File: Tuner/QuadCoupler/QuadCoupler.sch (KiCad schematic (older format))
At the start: 109 parts, among them J1 Conn_01x01, J10 Conn_01x02, J11 Conn_01x01, J12 Conn_01x01, J13 Conn_01x01, J14 Conn_01x01, J15 Conn_01x01, J16 Conn_01x01, J17 Conn_01x01, J19 Conn_01x02, J2 Conn_Coaxial, J21 Conn_01x01, J22 Conn_01x01, J23 Conn_01x01, J24 Conn_01x01, J3 Conn_Coaxial, J4 Conn_Coaxial, J5 Conn_Coaxial, J6 Conn_Coaxial, J7 Conn_01x01, J8 Conn_01x01, J9 Conn_01x01

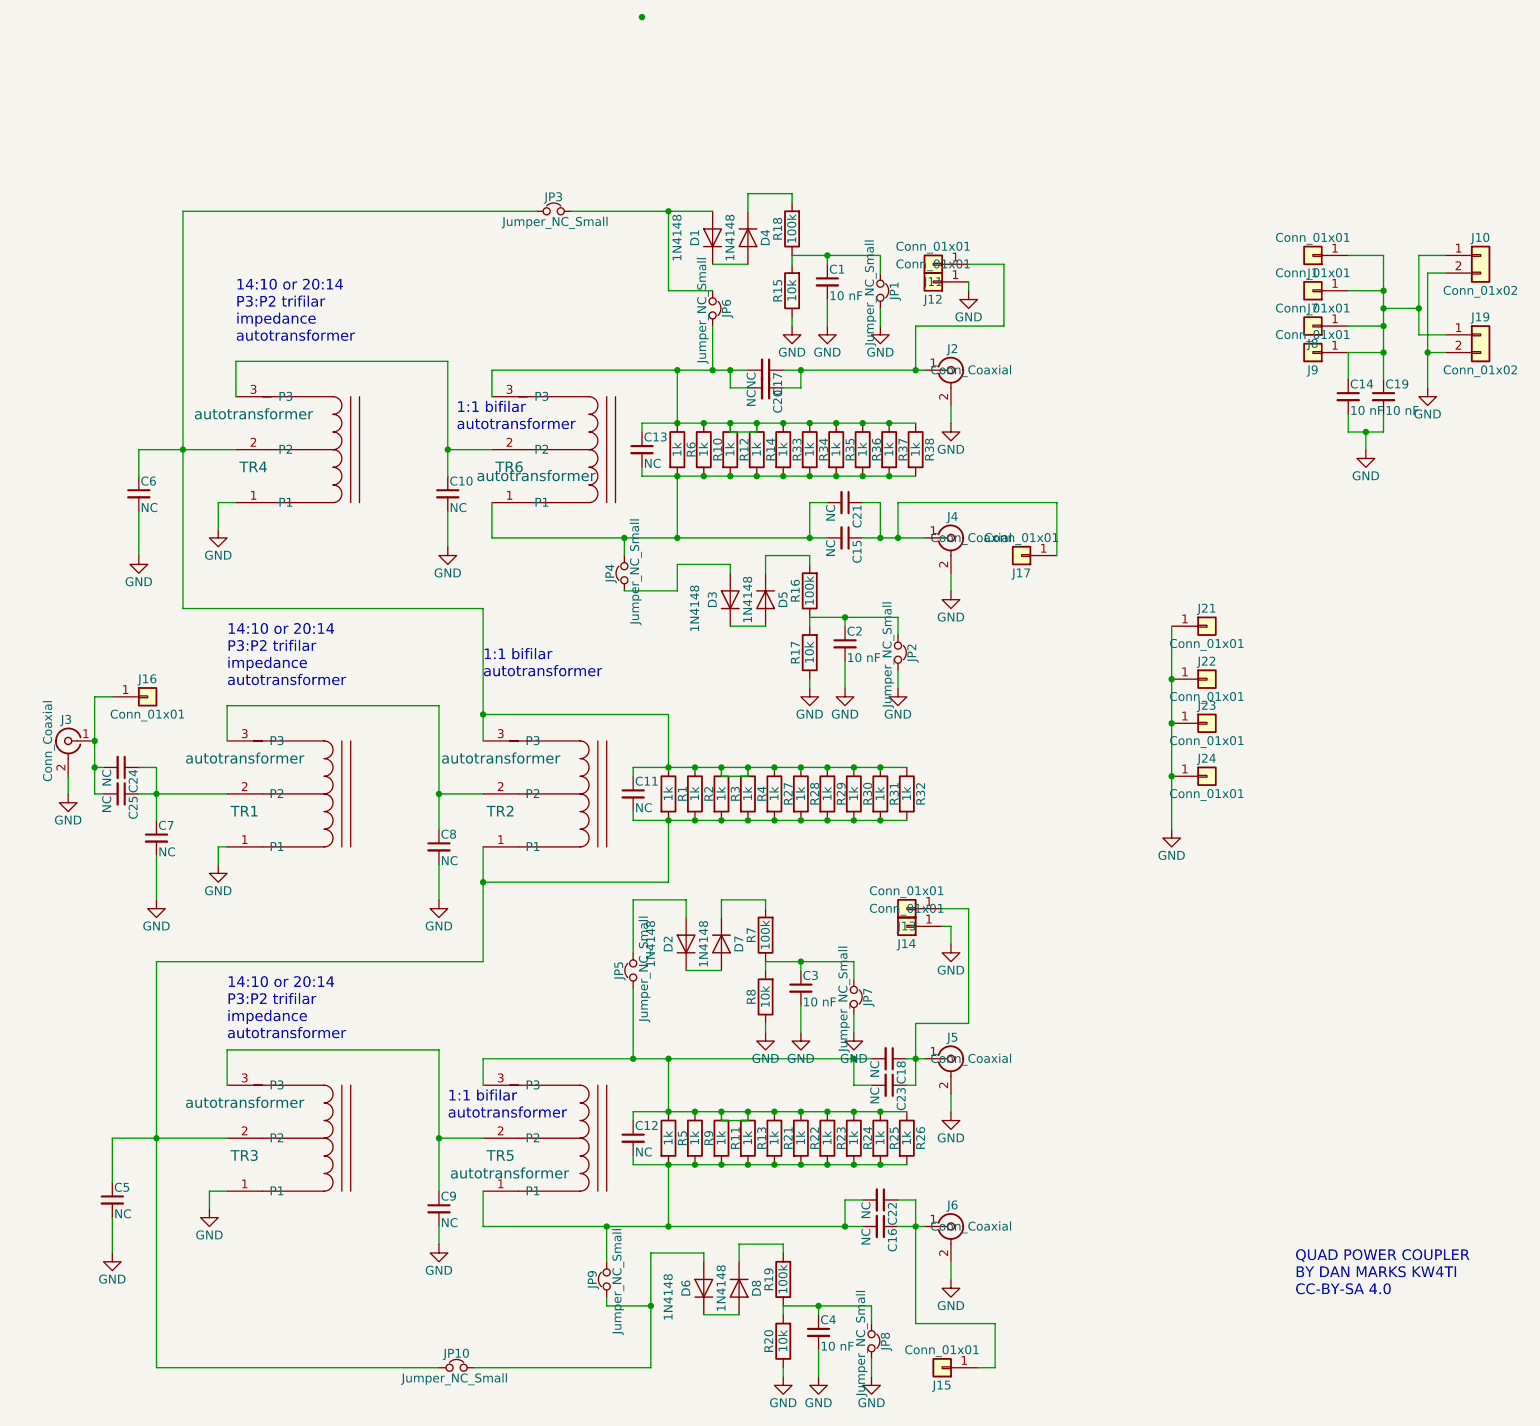
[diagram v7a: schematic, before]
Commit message: Change named to DirectionalCoupler, fixed order of two pins in QuadCoupler
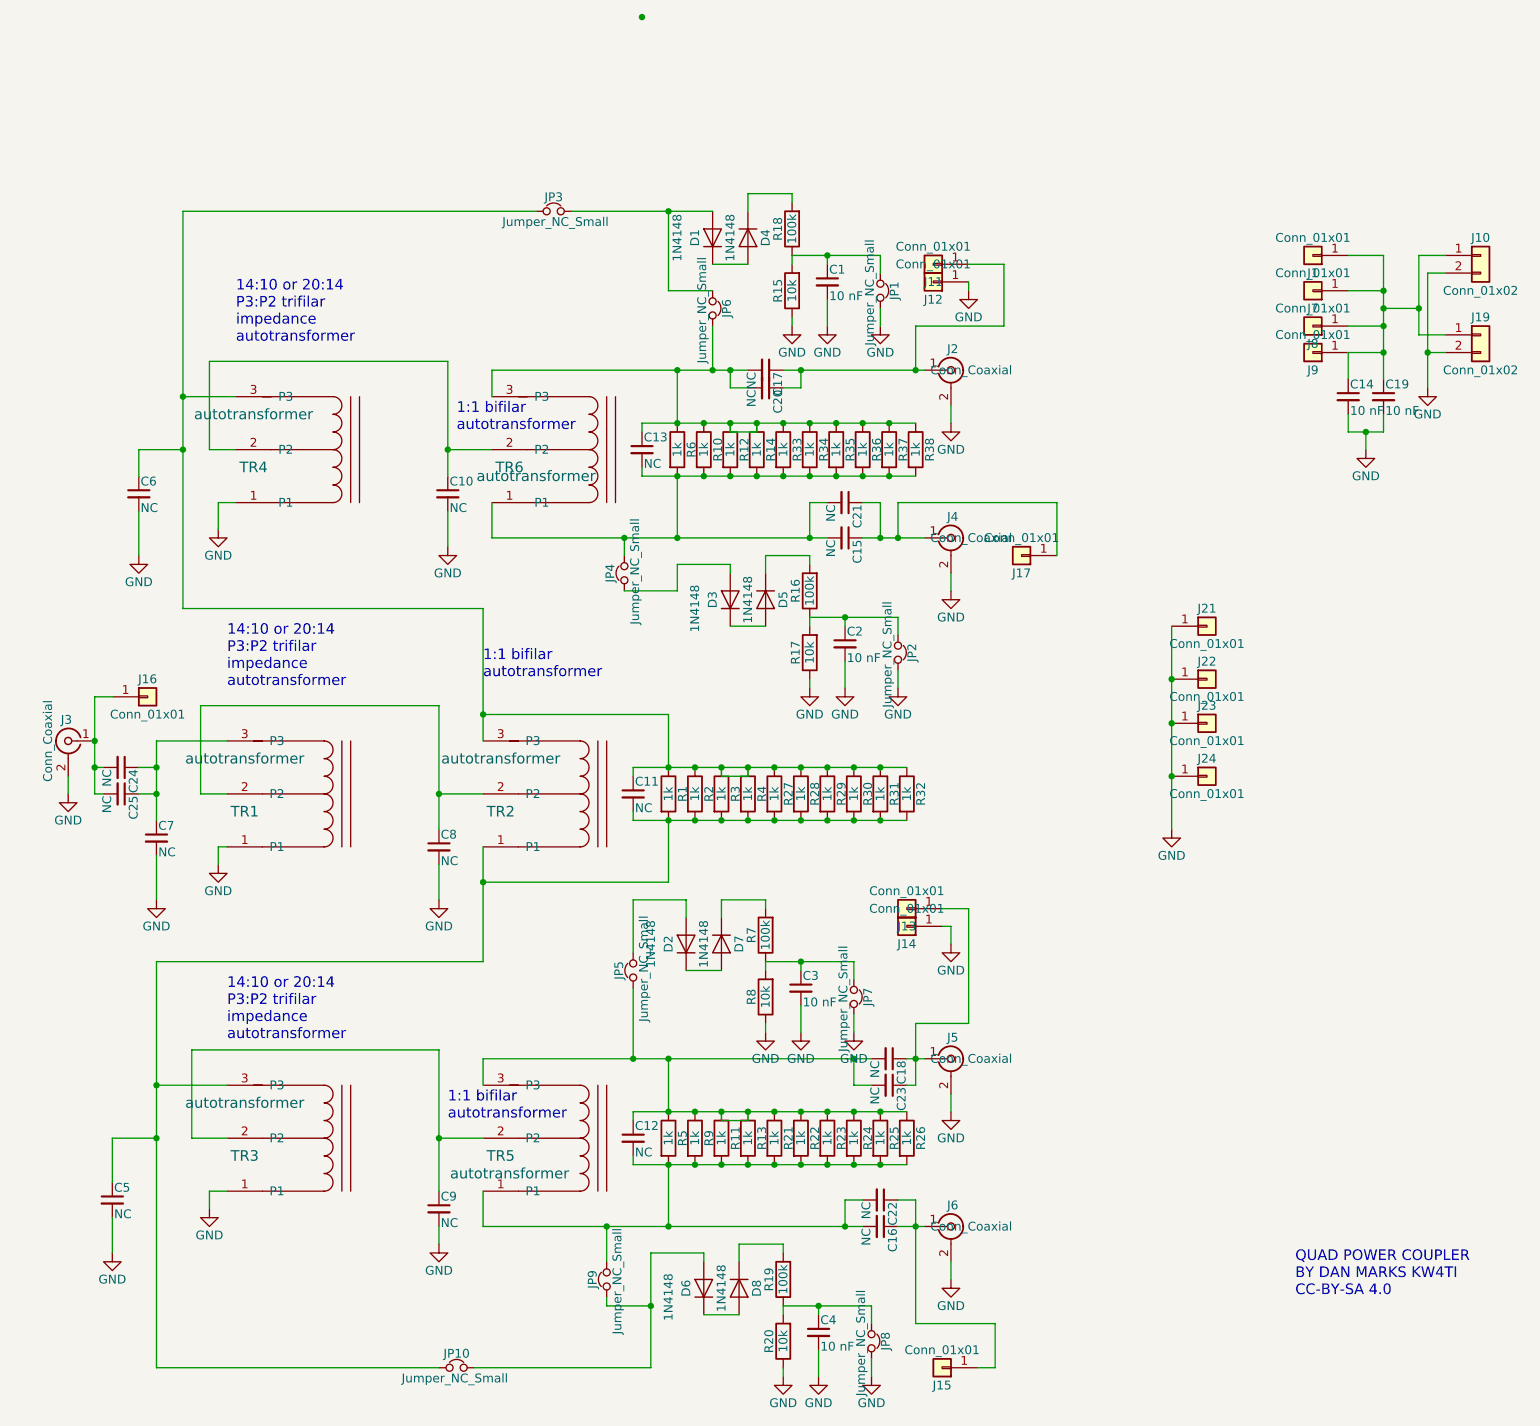
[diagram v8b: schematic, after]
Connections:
- net at C24.1, C25.1, C7.1: now also TR1.3 (P3); no longer TR1.2 (P2)
- net at C8.1, TR2.2 (P2): now also TR1.2 (P2); no longer TR1.3 (P3)
- net at C11.2, C5.1, JP10.2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: now also TR3.3 (P3); no longer TR3.2 (P2)
- net at C11.1, C6.1, JP3.1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: now also TR4.3 (P3); no longer TR4.2 (P2)
- net at C10.1, TR6.2 (P2): now also TR4.2 (P2); no longer TR4.3 (P3)
- net at C9.1, TR5.2 (P2): now also TR3.2 (P2); no longer TR3.3 (P3)
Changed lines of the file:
@@
 $EndComp
 $Comp
-L GND #PWR29
+L GND #PWR01
 U 1 1 5C69E7D4
 P 7000 4350
-F 0 "#PWR29" H 7000 4100 50  0001 C CNN
+F 0 "#PWR01" H 7000 4100 50  0001 C CNN
 F 1 "GND" H 7000 4200 50  0000 C CNN
 F 2 "" H 7000 4350 50  0001 C CNN
@@
 $EndComp
 $Comp
-L GND #PWR7
+L GND #PWR02
 U 1 1 5C721A79
 P 1600 4550
-F 0 "#PWR7" H 1600 4300 50  0001 C CNN
+F 0 "#PWR02" H 1600 4300 50  0001 C CNN
 F 1 "GND" H 1600 4400 50  0000 C CNN
 F 2 "" H 1600 4550 50  0001 C CNN
@@
 $EndComp
 $Comp
-L GND #PWR1
+L GND #PWR03
 U 1 1 5C721C63
 P 750 4150
-F 0 "#PWR1" H 750 3900 50  0001 C CNN
+F 0 "#PWR03" H 750 3900 50  0001 C CNN
 F 1 "GND" H 750 4000 50  0000 C CNN
 F 2 "" H 750 4150 50  0001 C CNN
@@
 1:1 bifilar\nautotransformer
 $Comp
-L GND #PWR6
+L GND #PWR04
 U 1 1 5C722D7A
 P 1600 2650
-F 0 "#PWR6" H 1600 2400 50  0001 C CNN
+F 0 "#PWR04" H 1600 2400 50  0001 C CNN
 F 1 "GND" H 1600 2500 50  0000 C CNN
 F 2 "" H 1600 2650 50  0001 C CNN
@@
 1:1 bifilar\nautotransformer
 $Comp
-L GND #PWR5
+L GND #PWR05
 U 1 1 5C722FF5
 P 1550 6500
-F 0 "#PWR5" H 1550 6250 50  0001 C CNN
+F 0 "#PWR05" H 1550 6250 50  0001 C CNN
 F 1 "GND" H 1550 6350 50  0000 C CNN
 F 2 "" H 1550 6500 50  0001 C CNN
@@
 $EndComp
 $Comp
-L GND #PWR23
+L GND #PWR06
 U 1 1 5C723AE4
 P 5750 2050
-F 0 "#PWR23" H 5750 1800 50  0001 C CNN
+F 0 "#PWR06" H 5750 1800 50  0001 C CNN
 F 1 "GND" H 5750 1900 50  0000 C CNN
 F 2 "" H 5750 2050 50  0001 C CNN
@@
 $EndComp
 $Comp
-L GND #PWR24
+L GND #PWR07
 U 1 1 5C72451D
 P 5750 3000
-F 0 "#PWR24" H 5750 2750 50  0001 C CNN
+F 0 "#PWR07" H 5750 2750 50  0001 C CNN
 F 1 "GND" H 5750 2850 50  0000 C CNN
 F 2 "" H 5750 3000 50  0001 C CNN
@@
 $EndComp
 $Comp
-L GND #PWR26
+L GND #PWR08
 U 1 1 5C7248D8
 P 5750 5950
-F 0 "#PWR26" H 5750 5700 50  0001 C CNN
+F 0 "#PWR08" H 5750 5700 50  0001 C CNN
 F 1 "GND" H 5750 5800 50  0000 C CNN
 F 2 "" H 5750 5950 50  0001 C CNN
@@
 $EndComp
 $Comp
-L GND #PWR27
+L GND #PWR09
 U 1 1 5C7248F8
 P 5750 6900
-F 0 "#PWR27" H 5750 6650 50  0001 C CNN
+F 0 "#PWR09" H 5750 6650 50  0001 C CNN
 F 1 "GND" H 5750 6750 50  0000 C CNN
 F 2 "" H 5750 6900 50  0001 C CNN
@@
 $EndComp
 $Comp
-L GND #PWR18
+L GND #PWR010
 U 1 1 5C725A72
 P 5150 3550
-F 0 "#PWR18" H 5150 3300 50  0001 C CNN
+F 0 "#PWR010" H 5150 3300 50  0001 C CNN
 F 1 "GND" H 5150 3400 50  0000 C CNN
 F 2 "" H 5150 3550 50  0001 C CNN
@@
 $EndComp
 $Comp
-L GND #PWR15
+L GND #PWR011
 U 1 1 5C7263A1
 P 4950 3550
-F 0 "#PWR15" H 4950 3300 50  0001 C CNN
+F 0 "#PWR011" H 4950 3300 50  0001 C CNN
 F 1 "GND" H 4950 3400 50  0000 C CNN
 F 2 "" H 4950 3550 50  0001 C CNN
@@
 $EndComp
 $Comp
-L GND #PWR22
+L GND #PWR012
 U 1 1 5C7266C0
 P 5450 3550
-F 0 "#PWR22" H 5450 3300 50  0001 C CNN
+F 0 "#PWR012" H 5450 3300 50  0001 C CNN
 F 1 "GND" H 5450 3400 50  0000 C CNN
 F 2 "" H 5450 3550 50  0001 C CNN
@@
 $EndComp
 $Comp
-L GND #PWR17
+L GND #PWR013
 U 1 1 5C726B07
 P 5050 1500
-F 0 "#PWR17" H 5050 1250 50  0001 C CNN
+F 0 "#PWR013" H 5050 1250 50  0001 C CNN
 F 1 "GND" H 5050 1350 50  0000 C CNN
 F 2 "" H 5050 1500 50  0001 C CNN
@@
 $EndComp
 $Comp
-L GND #PWR13
+L GND #PWR014
 U 1 1 5C726B1E
 P 4850 1500
-F 0 "#PWR13" H 4850 1250 50  0001 C CNN
+F 0 "#PWR014" H 4850 1250 50  0001 C CNN
 F 1 "GND" H 4850 1350 50  0000 C CNN
 F 2 "" H 4850 1500 50  0001 C CNN
@@
 $EndComp
 $Comp
-L GND #PWR21
+L GND #PWR015
 U 1 1 5C726B2C
 P 5350 1500
-F 0 "#PWR21" H 5350 1250 50  0001 C CNN
+F 0 "#PWR015" H 5350 1250 50  0001 C CNN
 F 1 "GND" H 5350 1350 50  0000 C CNN
 F 2 "" H 5350 1500 50  0001 C CNN
@@
 $EndComp
 $Comp
-L GND #PWR16
+L GND #PWR016
 U 1 1 5C728ED4
 P 5000 7450
-F 0 "#PWR16" H 5000 7200 50  0001 C CNN
+F 0 "#PWR016" H 5000 7200 50  0001 C CNN
 F 1 "GND" H 5000 7300 50  0000 C CNN
 F 2 "" H 5000 7450 50  0001 C CNN
@@
 $EndComp
 $Comp
-L GND #PWR12
+L GND #PWR017
 U 1 1 5C728EEB
 P 4800 7450
-F 0 "#PWR12" H 4800 7200 50  0001 C CNN
+F 0 "#PWR017" H 4800 7200 50  0001 C CNN
 F 1 "GND" H 4800 7300 50  0000 C CNN
 F 2 "" H 4800 7450 50  0001 C CNN
@@
 $EndComp
 $Comp
-L GND #PWR20
+L GND #PWR018
 U 1 1 5C728EF9
 P 5300 7450
-F 0 "#PWR20" H 5300 7200 50  0001 C CNN
+F 0 "#PWR018" H 5300 7200 50  0001 C CNN
 F 1 "GND" H 5300 7300 50  0000 C CNN
 F 2 "" H 5300 7450 50  0001 C CNN
@@
 $EndComp
 $Comp
-L GND #PWR14
+L GND #PWR019
 U 1 1 5C729631
 P 4900 5500
-F 0 "#PWR14" H 4900 5250 50  0001 C CNN
+F 0 "#PWR019" H 4900 5250 50  0001 C CNN
 F 1 "GND" H 4900 5350 50  0000 C CNN
 F 2 "" H 4900 5500 50  0001 C CNN
@@
 $EndComp
 $Comp
-L GND #PWR11
+L GND #PWR020
 U 1 1 5C729648
 P 4700 5500
-F 0 "#PWR11" H 4700 5250 50  0001 C CNN
+F 0 "#PWR020" H 4700 5250 50  0001 C CNN
 F 1 "GND" H 4700 5350 50  0000 C CNN
 F 2 "" H 4700 5500 50  0001 C CNN
@@
 $EndComp
 $Comp
-L GND #PWR19
+L GND #PWR021
 U 1 1 5C729656
 P 5200 5500
-F 0 "#PWR19" H 5200 5250 50  0001 C CNN
+F 0 "#PWR021" H 5200 5250 50  0001 C CNN
 F 1 "GND" H 5200 5350 50  0000 C CNN
 F 2 "" H 5200 5500 50  0001 C CNN
@@
 $EndComp
 $Comp
-L GND #PWR4
+L GND #PWR022
 U 1 1 5C74667B
 P 1250 4750
-F 0 "#PWR4" H 1250 4500 50  0001 C CNN
+F 0 "#PWR022" H 1250 4500 50  0001 C CNN
 F 1 "GND" H 1250 4600 50  0000 C CNN
 F 2 "" H 1250 4750 50  0001 C CNN
@@
 $EndComp
 $Comp
-L GND #PWR8
+L GND #PWR023
 U 1 1 5C747152
 P 2850 4750
-F 0 "#PWR8" H 2850 4500 50  0001 C CNN
+F 0 "#PWR023" H 2850 4500 50  0001 C CNN
 F 1 "GND" H 2850 4600 50  0000 C CNN
 F 2 "" H 2850 4750 50  0001 C CNN
@@
 $EndComp
 $Comp
-L GND #PWR3
+L GND #PWR024
 U 1 1 5C747AA2
 P 1150 2800
-F 0 "#PWR3" H 1150 2550 50  0001 C CNN
+F 0 "#PWR024" H 1150 2550 50  0001 C CNN
 F 1 "GND" H 1150 2650 50  0000 C CNN
 F 2 "" H 1150 2800 50  0001 C CNN
@@
 $EndComp
 $Comp
-L GND #PWR2
+L GND #PWR025
 U 1 1 5C748095
 P 1000 6750
-F 0 "#PWR2" H 1000 6500 50  0001 C CNN
+F 0 "#PWR025" H 1000 6500 50  0001 C CNN
 F 1 "GND" H 1000 6600 50  0000 C CNN
 F 2 "" H 1000 6750 50  0001 C CNN
@@
 $EndComp
 $Comp
-L GND #PWR9
+L GND #PWR026
 U 1 1 5C748BEC
 P 2850 6700
-F 0 "#PWR9" H 2850 6450 50  0001 C CNN
+F 0 "#PWR026" H 2850 6450 50  0001 C CNN
 F 1 "GND" H 2850 6550 50  0000 C CNN
 F 2 "" H 2850 6700 50  0001 C CNN
@@
 $EndComp
 $Comp
-L GND #PWR10
+L GND #PWR027
 U 1 1 5C749558
 P 2900 2750
-F 0 "#PWR10" H 2900 2500 50  0001 C CNN
+F 0 "#PWR027" H 2900 2500 50  0001 C CNN
 F 1 "GND" H 2900 2600 50  0000 C CNN
 F 2 "" H 2900 2750 50  0001 C CNN
@@
 $EndComp
 $Comp
-L GND #PWR28
+L GND #PWR028
 U 1 1 5C7B1635
 P 5850 1300
-F 0 "#PWR28" H 5850 1050 50  0001 C CNN
+F 0 "#PWR028" H 5850 1050 50  0001 C CNN
 F 1 "GND" H 5850 1150 50  0000 C CNN
 F 2 "" H 5850 1300 50  0001 C CNN
@@
 $EndComp
 $Comp
-L GND #PWR25
+L GND #PWR029
 U 1 1 5C7B20CD
 P 5750 5000
-F 0 "#PWR25" H 5750 4750 50  0001 C CNN
+F 0 "#PWR029" H 5750 4750 50  0001 C CNN
 F 1 "GND" H 5750 4850 50  0000 C CNN
 F 2 "" H 5750 5000 50  0001 C CNN
@@
 	1250 5100 1250 7400
 Wire Wire Line
-	1000 6100 1650 6100
+	1000 6100 1250 6100
 Wire Wire Line
 	3100 6600 5250 6600
@@
 	2850 5600 2850 6400
 Wire Wire Line
-	1650 5800 1650 5600
-Wire Wire Line
 	1550 6400 1650 6400
 Wire Wire Line
@@
 	1400 850  1400 3100
 Wire Wire Line
-	1150 2200 1700 2200
+	1150 2200 1400 2200
 Wire Wire Line
 	3150 2700 5050 2700
@@
 	2900 1700 2900 2350
 Wire Wire Line
-	1700 1900 1700 1700
-Wire Wire Line
 	1600 2500 1700 2500
 Wire Wire Line
@@
 	2850 3650 2850 4350
 Wire Wire Line
-	1650 3650 2850 3650
-Wire Wire Line
-	1650 3850 1650 3650
+	1500 3650 2850 3650
 Wire Wire Line
 	750  4150 750  4050
@@
 	4200 2700 4200 2350
 Wire Wire Line
-	1250 4000 1250 4300
+	1250 3850 1250 4300
 Connection ~ 1250 4150
 Wire Wire Line
@@
 	1600 4450 1600 4550
 Wire Wire Line
-	1650 5600 2850 5600
-Wire Wire Line
-	1700 1700 2900 1700
+	1450 5600 2850 5600
+Wire Wire Line
+	1550 1700 2900 1700
 Wire Wire Line
 	4050 7400 3050 7400
@@
 	8450 1200 8550 1200
 $Comp
-L GND #PWR31
+L GND #PWR030
 U 1 1 5C7E60AE
 P 8450 1850
-F 0 "#PWR31" H 8450 1600 50  0001 C CNN
+F 0 "#PWR030" H 8450 1600 50  0001 C CNN
 F 1 "GND" H 8450 1700 50  0000 C CNN
 F 2 "" H 8450 1850 50  0001 C CNN
@@
 $EndComp
 Wire Wire Line
-	8000 1650 8200 1650
+	8200 1650 8000 1650
 Wire Wire Line
 	8200 1100 8200 1800
@@
 	8000 1650 8000 1800
 Wire Wire Line
-	8200 2000 8200 2100
-Wire Wire Line
-	8200 2100 8000 2100
+	8200 2100 8200 2000
+Wire Wire Line
+	8000 2100 8200 2100
 Wire Wire Line
 	8000 2100 8000 2000
 $Comp
-L GND #PWR30
+L GND #PWR031
 U 1 1 5C7E92D6
 P 8100 2200
-F 0 "#PWR30" H 8100 1950 50  0001 C CNN
+F 0 "#PWR031" H 8100 1950 50  0001 C CNN
 F 1 "GND" H 8100 2050 50  0000 C CNN
 F 2 "" H 8100 2200 50  0001 C CNN
@@
 $EndComp
 Wire Wire Line
-	1150 4150 1650 4150
+	1150 4150 1250 4150
 Wire Wire Line
 	900  4150 950  4150
@@
 Text Notes 1650 5550 0    60   ~ 0
 14:10 or 20:14 \nP3:P2 trifilar\nimpedance\nautotransformer
+Wire Wire Line
+	1250 3850 1650 3850
+Connection ~ 1250 4000
+Wire Wire Line
+	1500 3650 1500 4150
+Wire Wire Line
+	1500 4150 1650 4150
+Wire Wire Line
+	1700 1900 1400 1900
+Connection ~ 1400 1900
+Wire Wire Line
+	1550 1700 1550 2200
+Wire Wire Line
+	1550 2200 1700 2200
+Wire Wire Line
+	1650 5800 1250 5800
+Connection ~ 1250 5800
+Wire Wire Line
+	1450 5600 1450 6100
+Wire Wire Line
+	1450 6100 1650 6100
 $EndSCHEMATC
